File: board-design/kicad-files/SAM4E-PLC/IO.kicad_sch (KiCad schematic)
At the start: 142 parts, among them Q10 BC807, Q11 BC807, Q12 BC807, Q3 BC807, Q4 BC807, Q5 BC807, Q6 BC807, Q7 BC807, Q8 BC807, Q9 BC807, U11 ULN2803CDWR, U12 74AC14SCX, U13 SN74HC240DBR

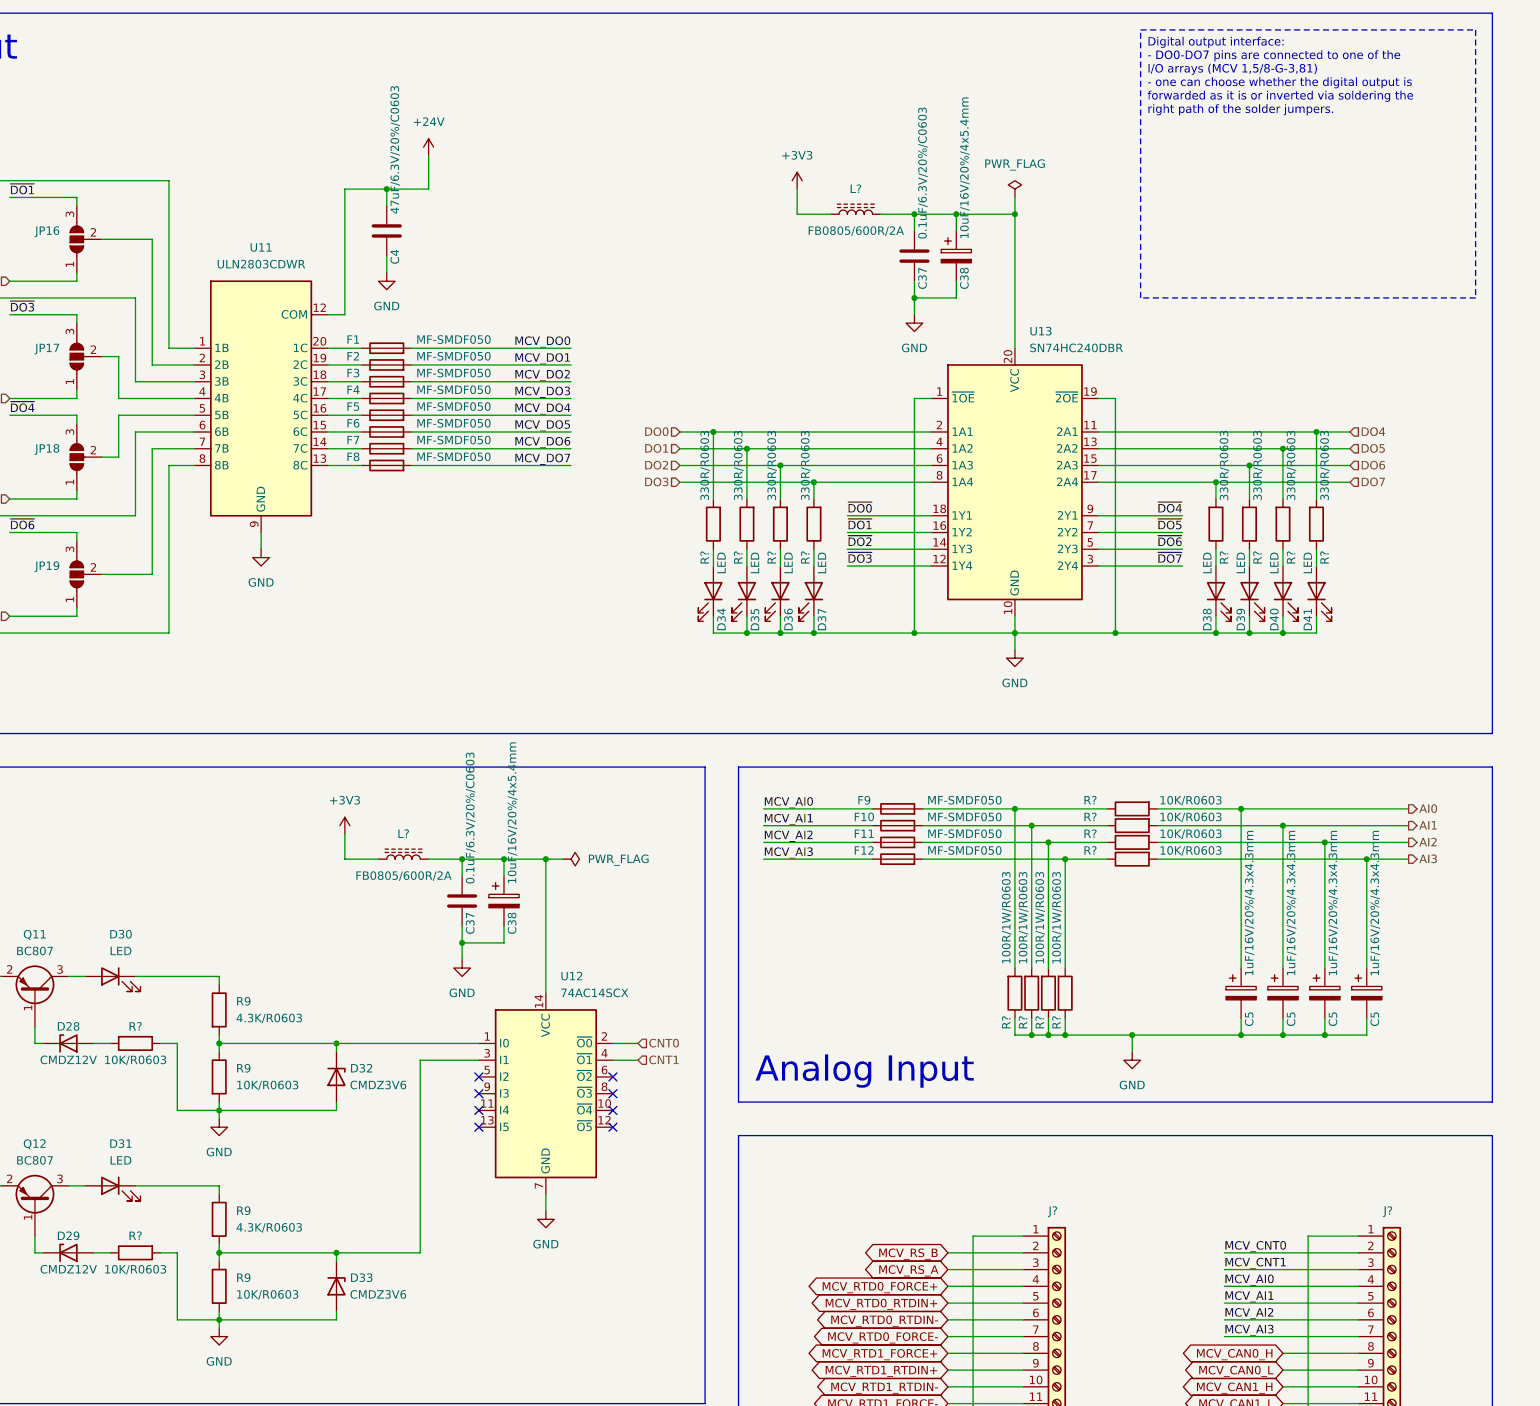
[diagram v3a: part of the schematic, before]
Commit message: [IN PROGRESS]
SAM4E-PLC PCB design in progress.

Signed-off-by: Nicolae-Andrei Vasile <vasilenicolaeandrei@gmail.com>
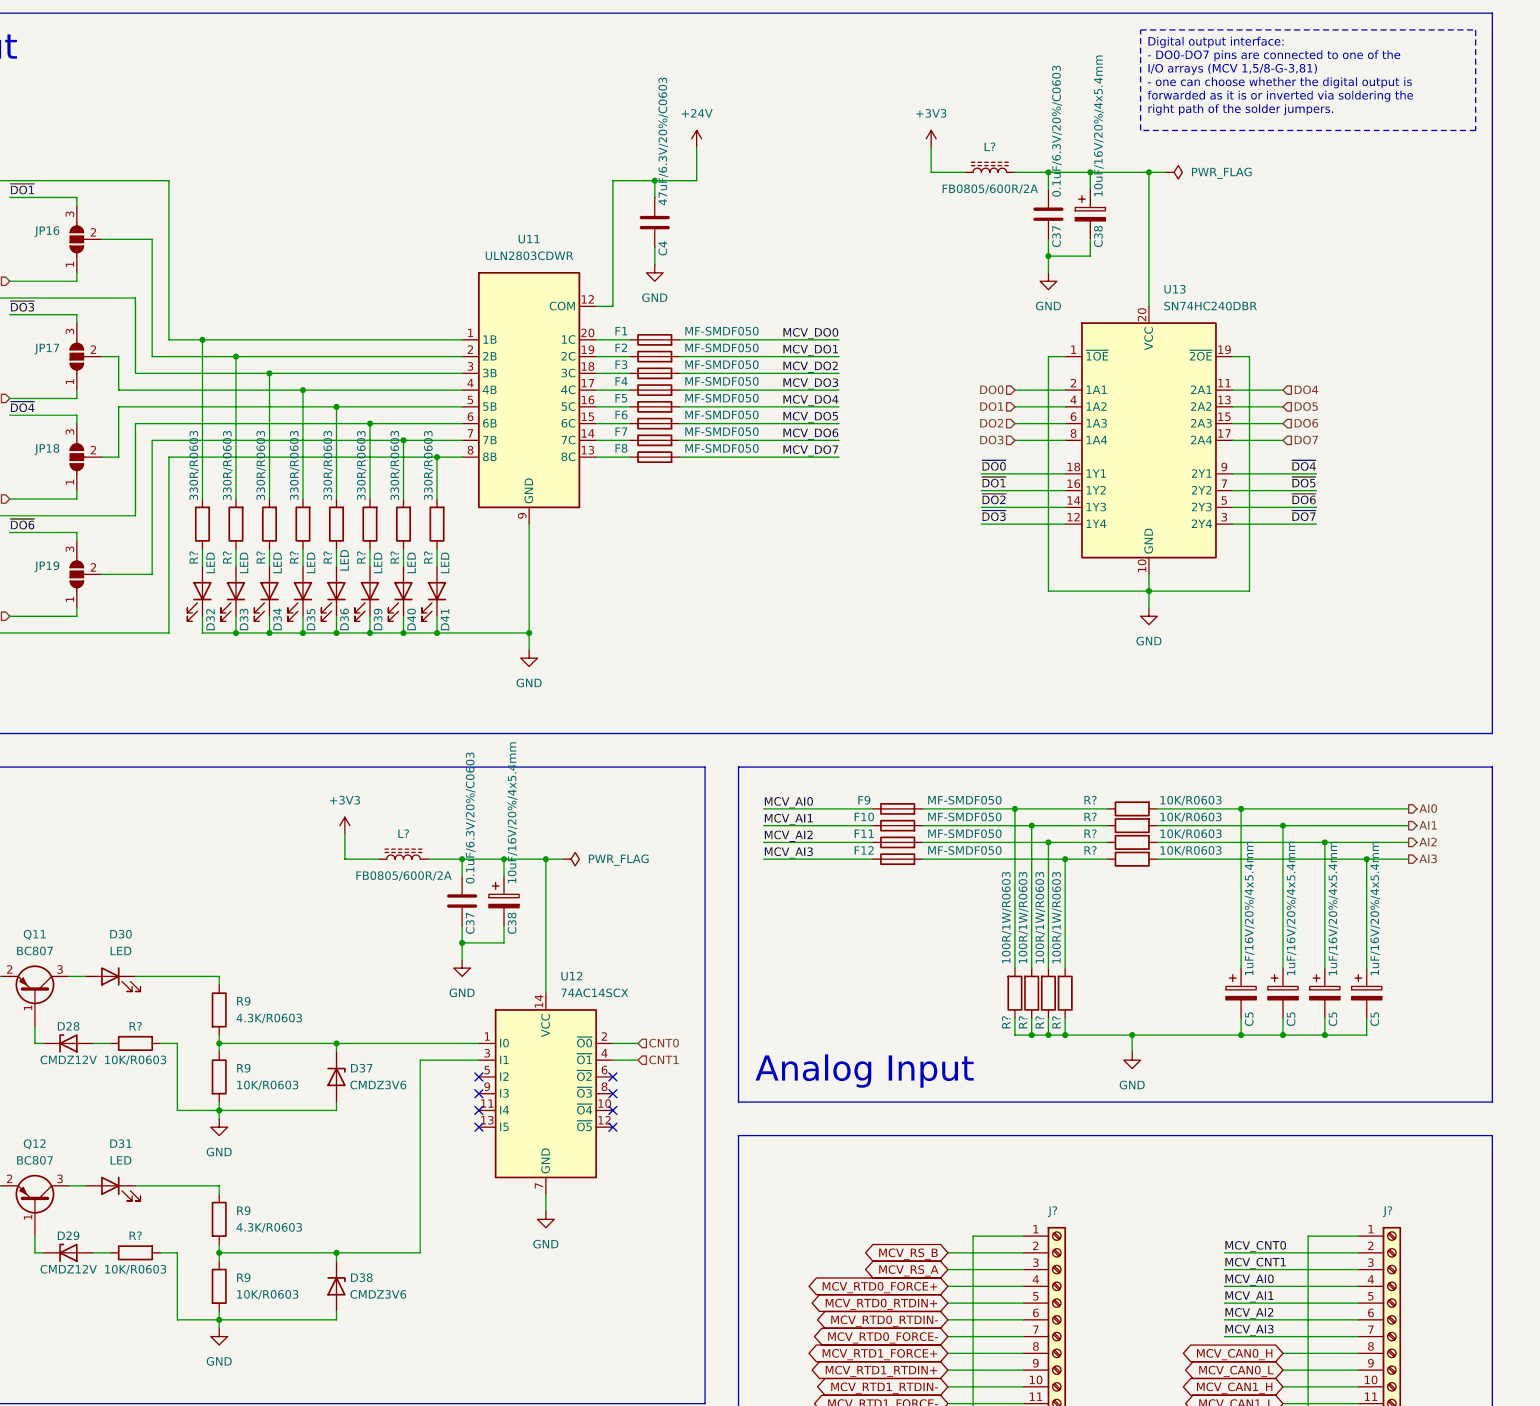
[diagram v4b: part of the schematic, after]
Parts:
- removed C5 (x3): 1uF/16V/20%/4.3x4.3mm, symbol Device:C_Polarized
- added C5 (x3): 1uF/16V/20%/4x5.4mm, Capacitor_SMD:CP_Elec_4x5.4, symbol Device:C_Polarized
- C5: value 1uF/16V/20%/4.3x4.3mm -> 1uF/16V/20%/4x5.4mm; footprint (none) -> Capacitor_SMD:CP_Elec_4x5.4
- renumbered D34 to D32, D35 to D33, D36 to D34, D37 to D35, D38 to D36, D32 to D37, D33 to D38
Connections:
- net AI1: now also C5.1
- net AI2: now also C5.1
- net AI3: now also C5.1
- net DO0: no longer R?.2
- net DO1: no longer R?.2
- net DO2: no longer R?.2
- net DO3: no longer R?.2
- net DO4: no longer R?.2
- net DO5: no longer R?.2
- net DO6: no longer R?.2
- net DO7: no longer R?.2
- net GND: now also C5.2, C5.2, C5.2
- net at JP13.2 (C), U11.3 (3B): now also R?.2
- net at JP18.2 (C), U11.5 (5B): now also R?.2
- net at JP15.2 (C), U11.8 (8B): now also R?.2
- net at JP12.2 (C), U11.1 (1B): now also R?.2
- net at JP19.2 (C), U11.7 (7B): now also R?.2
- net at JP14.2 (C), U11.6 (6B): now also R?.2
- net at JP17.2 (C), U11.4 (4B): now also R?.2
- net at JP16.2 (C), U11.2 (2B): now also R?.2
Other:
- moved on the sheet: C37, C38, C4, D32, D33, D34, D35, D36, D39, D40, D41, F1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

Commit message: [UPDATE]
Work in progress.

Signed-off-by: Nicolae-Andrei Vasile <vasilenicolaeandrei@gmail.com>
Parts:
- removed D32, D33, D34, D35, D36, D39, D40, D41: LED, LED_SMD:LED_0805_2012Metric, symbol Device:LED
- removed R? (x8): 330R/R0603, Resistor_SMD:R_0603_1608Metric, symbol Device:R
- renumbered D9 to D10, D10 to D11, D11 to D12, D12 to D13, D13 to D14, D14 to D15, D15 to D16, D16 to D17, D17 to D18, D18 to D19, D19 to D20, D20 to D21, D21 to D22, D22 to D23, D23 to D24, D24 to D25, D25 to D26, D26 to D27, D27 to D28, D28 to D29, D29 to D30, D30 to D31, D31 to D32, D37 to D33, D38 to D34, D4 to D5, D5 to D6, D6 to D7, D7 to D8, D8 to D9, JP17 to JP12, JP16 to JP13, JP19 to JP14, JP18 to JP15, JP13 to JP16, JP12 to JP17, JP15 to JP18, JP14 to JP19
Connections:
- net MCV_DO0: now also F4.2, J?.7 (Pin_7); no longer F1.2, J?.4 (Pin_4)
- net MCV_DO1: now also F3.2; no longer F2.2
- net MCV_DO2: now also F2.2; no longer F3.2
- net MCV_DO3: now also F1.2, J?.4 (Pin_4); no longer F4.2, J?.7 (Pin_7)
- net MCV_DO4: now also F8.2, J?.11 (Pin_11); no longer F5.2, J?.8 (Pin_8)
- net MCV_DO5: now also F7.2, J?.10 (Pin_10); no longer F6.2, J?.9 (Pin_9)
- net MCV_DO6: now also F6.2, J?.9 (Pin_9); no longer F7.2, J?.10 (Pin_10)
- net MCV_DO7: now also F5.2, J?.8 (Pin_8); no longer F8.2, J?.11 (Pin_11)
- net MCV_RTD0_FORCE+: now also J?.7 (Pin_7); no longer J?.4 (Pin_4)
- net MCV_RTD0_FORCE-: now also J?.4 (Pin_4); no longer J?.7 (Pin_7)
- net MCV_RTD0_RTDIN+: now also J?.6 (Pin_6); no longer J?.5 (Pin_5)
- net MCV_RTD0_RTDIN-: now also J?.5 (Pin_5); no longer J?.6 (Pin_6)
- net MCV_RTD1_FORCE+: now also J?.11 (Pin_11); no longer J?.8 (Pin_8)
- net MCV_RTD1_FORCE-: now also J?.8 (Pin_8); no longer J?.11 (Pin_11)
- net MCV_RTD1_RTDIN+: now also J?.10 (Pin_10); no longer J?.9 (Pin_9)
- net MCV_RTD1_RTDIN-: now also J?.9 (Pin_9); no longer J?.10 (Pin_10)
- net at JP16.2 (C): now also U11.2 (2B); no longer U11.3 (3B)
- net at JP15.2 (C): now also U11.8 (8B); no longer U11.5 (5B)
- net at JP18.2 (C): now also U11.5 (5B); no longer U11.8 (8B)
- net at U11.4 (4B): now also JP17.2 (C); no longer JP12.2 (C)
- net at U11.1 (1B): now also JP12.2 (C); no longer JP17.2 (C)
- net at JP14.2 (C): now also U11.6 (6B); no longer U11.7 (7B)
- net at JP19.2 (C): now also U11.7 (7B); no longer U11.6 (6B)
- net at JP13.2 (C): now also U11.3 (3B); no longer U11.2 (2B)
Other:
- moved on the sheet: C37, C38, C4, F1, F2, F3, F4, F5, F6, F7, F8, JP12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

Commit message: [UPDATE]
Work in progress.

Signed-off-by: Nicolae-Andrei Vasile <vasilenicolaeandrei@gmail.com>
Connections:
- net AI0: now also C5.1, R?.2; no longer C5.1, R?.2
- net AI1: now also C5.1, R?.2; no longer C5.1, R?.2
- net AI2: now also C5.1, R?.2; no longer C5.1, R?.2
- net AI3: now also C5.1, R?.2; no longer C5.1, R?.2
- net MCV_AI0: now also F12.1, J?.7 (Pin_7); no longer F9.1, J?.4 (Pin_4)
- net MCV_AI1: now also F11.1, J?.6 (Pin_6); no longer F10.1, J?.5 (Pin_5)
- net MCV_AI2: now also F10.1, J?.5 (Pin_5); no longer F11.1, J?.6 (Pin_6)
- net MCV_AI3: now also F9.1, J?.4 (Pin_4); no longer F12.1, J?.7 (Pin_7)
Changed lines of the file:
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@@
     (effects (font (size 3.81 3.81) (color 140 140 0 1)) (justify left bottom))
   )
-  (label "MCV_AI3" (at 292.1 146.05 0) (fields_autoplaced)
+  (label "MCV_AI3" (at 292.1 138.43 0) (fields_autoplaced)
     (effects (font (size 1.27 1.27)) (justify left bottom))
   )
@@
     (effects (font (size 1.27 1.27)) (justify left bottom))
   )
-  (label "MCV_AI2" (at 361.95 215.9 0) (fields_autoplaced)
+  (label "MCV_AI2" (at 361.95 213.36 0) (fields_autoplaced)
     (effects (font (size 1.27 1.27)) (justify left bottom))
   )
-  (label "MCV_AI0" (at 361.95 210.82 0) (fields_autoplaced)
+  (label "MCV_AI0" (at 361.95 218.44 0) (fields_autoplaced)
     (effects (font (size 1.27 1.27)) (justify left bottom))
   )
@@
     (effects (font (size 1.27 1.27)) (justify left bottom))
   )
-  (label "MCV_AI0" (at 292.1 138.43 0) (fields_autoplaced)
+  (label "MCV_AI0" (at 292.1 146.05 0) (fields_autoplaced)
     (effects (font (size 1.27 1.27)) (justify left bottom))
   )
-  (label "MCV_AI3" (at 361.95 218.44 0) (fields_autoplaced)
+  (label "MCV_AI3" (at 361.95 210.82 0) (fields_autoplaced)
     (effects (font (size 1.27 1.27)) (justify left bottom))
   )
@@
     (effects (font (size 1.27 1.27)) (justify left bottom))
   )
-  (label "MCV_AI1" (at 292.1 140.97 0) (fields_autoplaced)
+  (label "MCV_AI1" (at 292.1 143.51 0) (fields_autoplaced)
     (effects (font (size 1.27 1.27)) (justify left bottom))
   )
@@
     (effects (font (size 1.27 1.27)) (justify left bottom))
   )
-  (label "MCV_AI1" (at 361.95 213.36 0) (fields_autoplaced)
+  (label "MCV_AI1" (at 361.95 215.9 0) (fields_autoplaced)
     (effects (font (size 1.27 1.27)) (justify left bottom))
   )
@@
     (effects (font (size 1.27 1.27)) (justify left bottom))
   )
-  (label "MCV_AI2" (at 292.1 143.51 0) (fields_autoplaced)
+  (label "MCV_AI2" (at 292.1 140.97 0) (fields_autoplaced)
     (effects (font (size 1.27 1.27)) (justify left bottom))
   )
@@
     (effects (font (size 1.27 1.27)) (justify left))
   )
-  (hierarchical_label "AI0" (shape output) (at 389.89 138.43 0) (fields_autoplaced)
+  (hierarchical_label "AI0" (shape output) (at 389.89 146.05 0) (fields_autoplaced)
     (effects (font (size 1.27 1.27)) (justify left))
   )
-  (hierarchical_label "AI1" (shape output) (at 389.89 140.97 0) (fields_autoplaced)
+  (hierarchical_label "AI1" (shape output) (at 389.89 143.51 0) (fields_autoplaced)
     (effects (font (size 1.27 1.27)) (justify left))
   )
@@
     (effects (font (size 1.27 1.27)) (justify right))
   )
-  (hierarchical_label "AI3" (shape output) (at 389.89 146.05 0) (fields_autoplaced)
+  (hierarchical_label "AI3" (shape output) (at 389.89 138.43 0) (fields_autoplaced)
     (effects (font (size 1.27 1.27)) (justify left))
   )
@@
     (effects (font (size 1.27 1.27)) (justify left))
   )
-  (hierarchical_label "AI2" (shape output) (at 389.89 143.51 0) (fields_autoplaced)
+  (hierarchical_label "AI2" (shape output) (at 389.89 140.97 0) (fields_autoplaced)
     (effects (font (size 1.27 1.27)) (justify left))
   )
@@
         )
         (path "/93076d8a-73da-4f5d-b7f2-28678f1db77d/f76e13f7-6a24-4ea6-98c5-a4d0bd3b3ced"
-          (reference "C86") (unit 1)
+          (reference "C87") (unit 1)
         )
       )
@@
         )
         (path "/93076d8a-73da-4f5d-b7f2-28678f1db77d/f76e13f7-6a24-4ea6-98c5-a4d0bd3b3ced"
-          (reference "C87") (unit 1)
+          (reference "C88") (unit 1)
         )
       )
@@
         )
         (path "/93076d8a-73da-4f5d-b7f2-28678f1db77d/f76e13f7-6a24-4ea6-98c5-a4d0bd3b3ced"
-          (reference "C80") (unit 1)
+          (reference "C81") (unit 1)
         )
       )
@@
         )
         (path "/93076d8a-73da-4f5d-b7f2-28678f1db77d/f76e13f7-6a24-4ea6-98c5-a4d0bd3b3ced"
-          (reference "C83") (unit 1)
+          (reference "C84") (unit 1)
         )
       )
@@
         )
         (path "/93076d8a-73da-4f5d-b7f2-28678f1db77d/f76e13f7-6a24-4ea6-98c5-a4d0bd3b3ced"
-          (reference "C79") (unit 1)
+          (reference "C80") (unit 1)
         )
       )
@@
         )
         (path "/93076d8a-73da-4f5d-b7f2-28678f1db77d/f76e13f7-6a24-4ea6-98c5-a4d0bd3b3ced"
-          (reference "C85") (unit 1)
+          (reference "C86") (unit 1)
         )
       )
@@
         )
         (path "/93076d8a-73da-4f5d-b7f2-28678f1db77d/f76e13f7-6a24-4ea6-98c5-a4d0bd3b3ced"
-          (reference "C81") (unit 1)
+          (reference "C82") (unit 1)
         )
       )
@@
         )
         (path "/93076d8a-73da-4f5d-b7f2-28678f1db77d/f76e13f7-6a24-4ea6-98c5-a4d0bd3b3ced"
-          (reference "C84") (unit 1)
+          (reference "C85") (unit 1)
         )
       )
@@
         )
         (path "/93076d8a-73da-4f5d-b7f2-28678f1db77d/f76e13f7-6a24-4ea6-98c5-a4d0bd3b3ced"
-          (reference "C82") (unit 1)
+          (reference "C83") (unit 1)
         )
       )

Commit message: [UPDATE]
Work in progress.

Signed-off-by: Nicolae-Andrei Vasile <vasilenicolaeandrei@gmail.com>
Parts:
- renumbered D9 to D10, D10 to D11, D11 to D12, D12 to D13, D13 to D14, D14 to D15, D15 to D16, D16 to D17, D17 to D18, D18 to D19, D19 to D20, D20 to D21, D21 to D22, D22 to D23, D23 to D24, D24 to D25, D25 to D26, D26 to D27, D27 to D28, D28 to D29, D29 to D31, D31 to D33, D33 to D35, D5 to D6, D6 to D7, D7 to D8, D8 to D9, Q12 to Q11, Q11 to Q12
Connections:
- net MCV_CAN0_H: now also J?.10 (Pin_10); no longer J?.8 (Pin_8)
- net MCV_CAN0_L: now also J?.11 (Pin_11); no longer J?.9 (Pin_9)
- net MCV_CAN1_H: now also J?.8 (Pin_8); no longer J?.10 (Pin_10)
- net MCV_CAN1_L: now also J?.9 (Pin_9); no longer J?.11 (Pin_11)
- net at D34.1 (K), R9.1, R9.2: now also U12.1 (I0); no longer U12.3 (I1)
- net at D35.1 (K), R9.1, R9.2: now also U12.3 (I1); no longer U12.1 (I0)
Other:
- moved on the sheet: D30, D31, D32, D33, D34, D35, Q11, Q12, R9, R?

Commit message: [UPDATE]
Work in progress.

Signed-off-by: Nicolae-Andrei Vasile <vasilenicolaeandrei@gmail.com>
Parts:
- renumbered D12 to D10, D13 to D11, D14 to D12, D15 to D13, D16 to D14, D17 to D15, D18 to D16, D19 to D17, D20 to D18, D21 to D19, D22 to D20, D23 to D21, D24 to D22, D25 to D23, D26 to D24, D27 to D25, D28 to D26, D29 to D27, D30 to D28, D31 to D29, D32 to D30, D33 to D31, D34 to D32, D35 to D33, D6 to D4, D7 to D5, D8 to D6, D9 to D7, D10 to D8, D11 to D9, JP12 to JP13, JP13 to JP14, JP14 to JP15, JP15 to JP16, JP16 to JP17, JP17 to JP18, JP18 to JP19, JP19 to JP20, Q3 to Q1, Q12 to Q10, Q4 to Q2, Q5 to Q3, Q6 to Q4, Q7 to Q5, Q8 to Q6, Q9 to Q7, Q10 to Q8, Q11 to Q9, U13 to U10, U11 to U8, U12 to U9
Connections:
- net MCV_DO1: now also J?.6 (Pin_6); no longer J?.5 (Pin_5)
- net MCV_DO2: now also J?.5 (Pin_5); no longer J?.6 (Pin_6)
